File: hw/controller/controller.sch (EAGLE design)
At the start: 76 parts, among them J1 JST-PH3SMT_VERT, J2 JST-PH3SMT_VERT, Q1 TPN1R603PL, Q2 TPN1R603PL, Q3 TPN1R603PL, Q4 TPN1R603PL, Q5 TPN1R603PL, Q6 TPN1R603PL, U1 STM32F4R_64PIN, U2 DRV8323RS, U3 AS5147, U4 MAX13431E, X1 8.0MHz

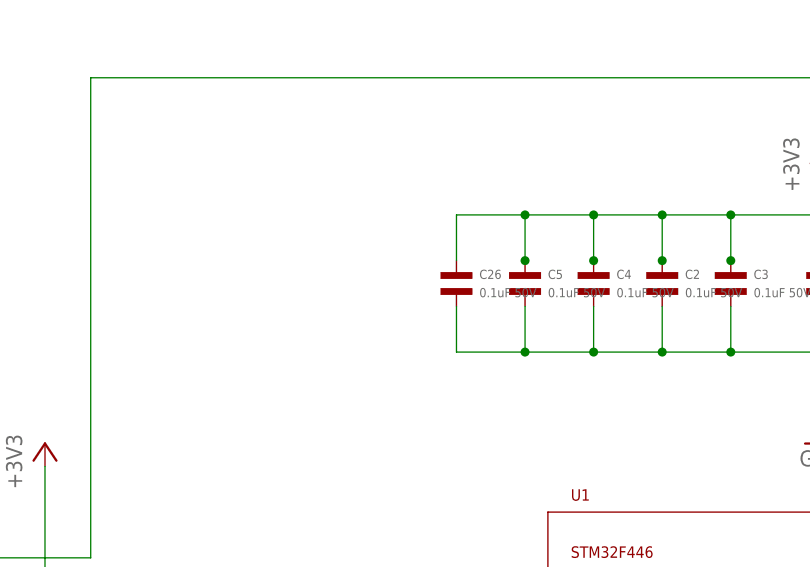
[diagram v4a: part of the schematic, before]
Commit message: More layout and schematic tweaks
 * Add a recommended 1uF bypass on the STM32 VDDA
 * Route VDRAIN on DRV8323 separately from VM
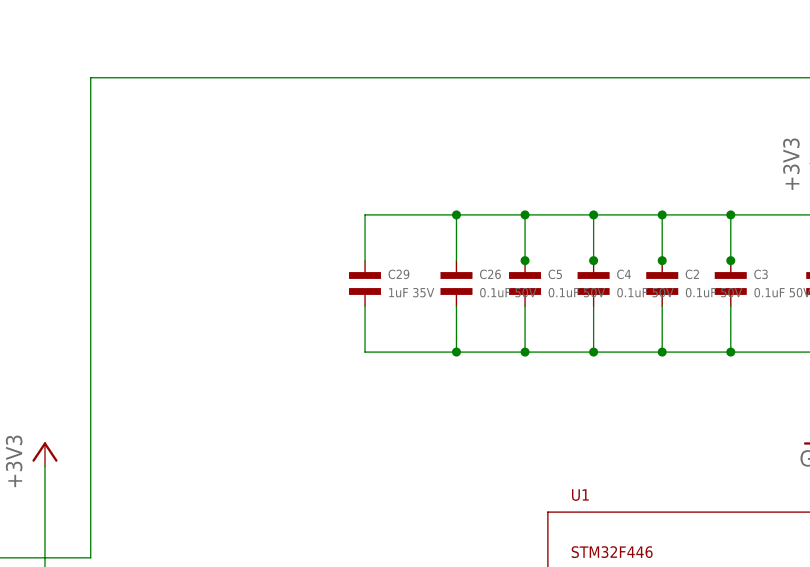
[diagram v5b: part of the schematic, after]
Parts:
- added C29: 1uF 35V, mfpassives:CAPACITOR_NP_0402
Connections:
- net +3V3: now also C29.P$1
- net GND: now also C29.P$2
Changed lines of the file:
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@@
 <attribute name="MPN" value="ERJ-2RKF1003X"/>
+</part>
+<part name="C29" library="mfpassives" deviceset="CAPACITOR_NP" device="_0402" value="1uF 35V">
+<attribute name="MF" value="Samsung Electro-Mechanics"/>
+<attribute name="MPN" value="CL05A105KL5NRNC"/>
 </part>
 </parts>
@@
 <attribute name="MPN" x="134.62" y="-330.2" size="1.778" layer="96" display="off"/>
 <attribute name="MF" x="134.62" y="-330.2" size="1.778" layer="96" display="off"/>
+</instance>
+<instance part="C29" gate="G$1" x="7.62" y="116.84">
+<attribute name="MPN" x="7.62" y="116.84" size="1.778" layer="96" display="off"/>
+<attribute name="MF" x="7.62" y="116.84" size="1.778" layer="96" display="off"/>
 </instance>
 </instances>
@@
 <wire x1="17.78" y1="124.46" x2="17.78" y2="119.38" width="0.1524" layer="91"/>
 <junction x="25.4" y="124.46"/>
+<pinref part="C29" gate="G$1" pin="P$1"/>
+<wire x1="7.62" y1="119.38" x2="7.62" y2="124.46" width="0.1524" layer="91"/>
+<wire x1="7.62" y1="124.46" x2="17.78" y2="124.46" width="0.1524" layer="91"/>
+<junction x="17.78" y="124.46"/>
 </segment>
 <segment>
@@
 <wire x1="17.78" y1="109.22" x2="25.4" y2="109.22" width="0.1524" layer="91"/>
 <junction x="25.4" y="109.22"/>
-</segment>
-<segment>
+<pinref part="C29" gate="G$1" pin="P$2"/>
+<wire x1="17.78" y1="109.22" x2="7.62" y2="109.22" width="0.1524" layer="91"/>
+<wire x1="7.62" y1="109.22" x2="7.62" y2="114.3" width="0.1524" layer="91"/>
+<junction x="17.78" y="109.22"/>
+</segment>
+<segment>

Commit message: Fix a number of r1 errata
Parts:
- removed ABS: PAD4, controller:PAD4
- added ABS_3V, ABS_GND, ABS_SCL, ABS_SDA: PAD24AWG_PAD, controller:PAD24AWG_PAD
- added C30: 1uF 35V, mfpassives:CAPACITOR_NP_0402
- added C31, C32: 0.1uF 50V, mfpassives:CAPACITOR_NP_0402
- added R12: 47k NTC, mfpassives:RESISTOR_0402
- added R13: 10k 1%, mfpassives:RESISTOR_0402
- added U5: MAX13433EETD+T, controller:MAX13433EETD+T
- DBG: value PAD4 -> JST-ZH6SMT_VERT; device controller:PAD4 -> controller:JST-ZH6SMT_VERT; MF (none) -> JST; MPN (none) -> B6B-ZR-SM4-TF(LF)(SN); POPULATE 0 -> 1
- SWD: value JST-ZH6 -> JST-ZH6SMT_VERT; device controller:JST-ZH6 -> controller:JST-ZH6SMT_VERT; MPN S6B-ZR-SM4A-TF(LF)(SN) -> B6B-ZR-SM4-TF(LF)(SN)
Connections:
- net VTEMP renamed VTEMP_MOT
- new net DBG_A: DBG.5, U5.A
- new net DBG_B: DBG.4, U5.B
- new net DBG_Y: DBG.2, U5.Y
- new net DBG_Z: DBG.3, U5.Z
- new net VTEMP_FET: C32.P$1, R12.P$2, R13.P$1, U1.PC2/SPI2_MISO
- net +3V3: now also ABS_3V.P$1, C30.P$1, C31.P$1, DBG.6, R12.P$1, U5.DE, U5.VL, U5.VSS; no longer ABS.1, DBG.1
- net DEBUG_RX: now also U5.RO; no longer DBG.3
- net DEBUG_TX: now also U5.DI; no longer DBG.2
- net GND: now also ABS_GND.P$1, C30.P$2, C31.P$2, C32.P$2, DBG.1, R13.P$2, U5.!RE, U5.EP, U5.GND, U5.GND_2; no longer ABS.4, DBG.4
- net I2C_ABS_SCL: now also ABS_SCL.P$1; no longer ABS.3
- net I2C_ABS_SDA: now also ABS_SDA.P$1; no longer ABS.2
